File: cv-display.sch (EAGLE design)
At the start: 21 parts, among them IC1 TL072JD, IC2 TL072JD

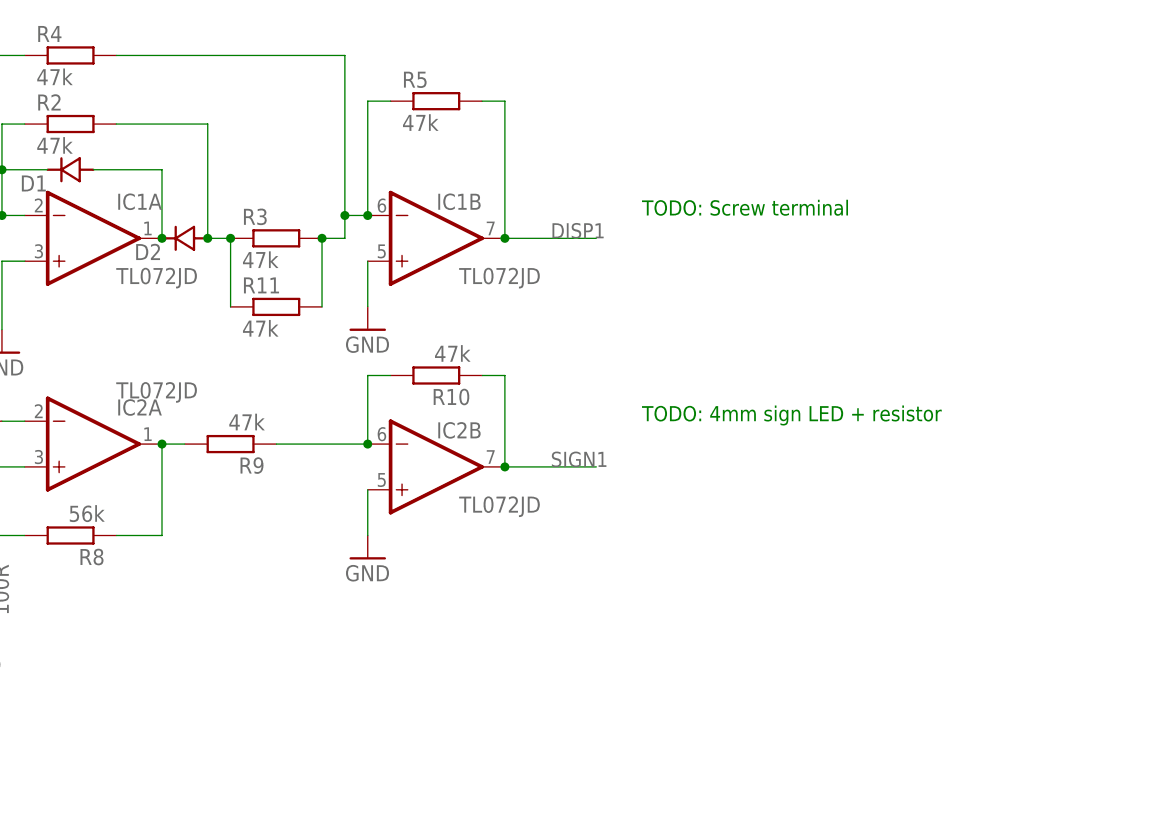
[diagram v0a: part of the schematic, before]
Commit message: Tested circuit, only missing screw terminals
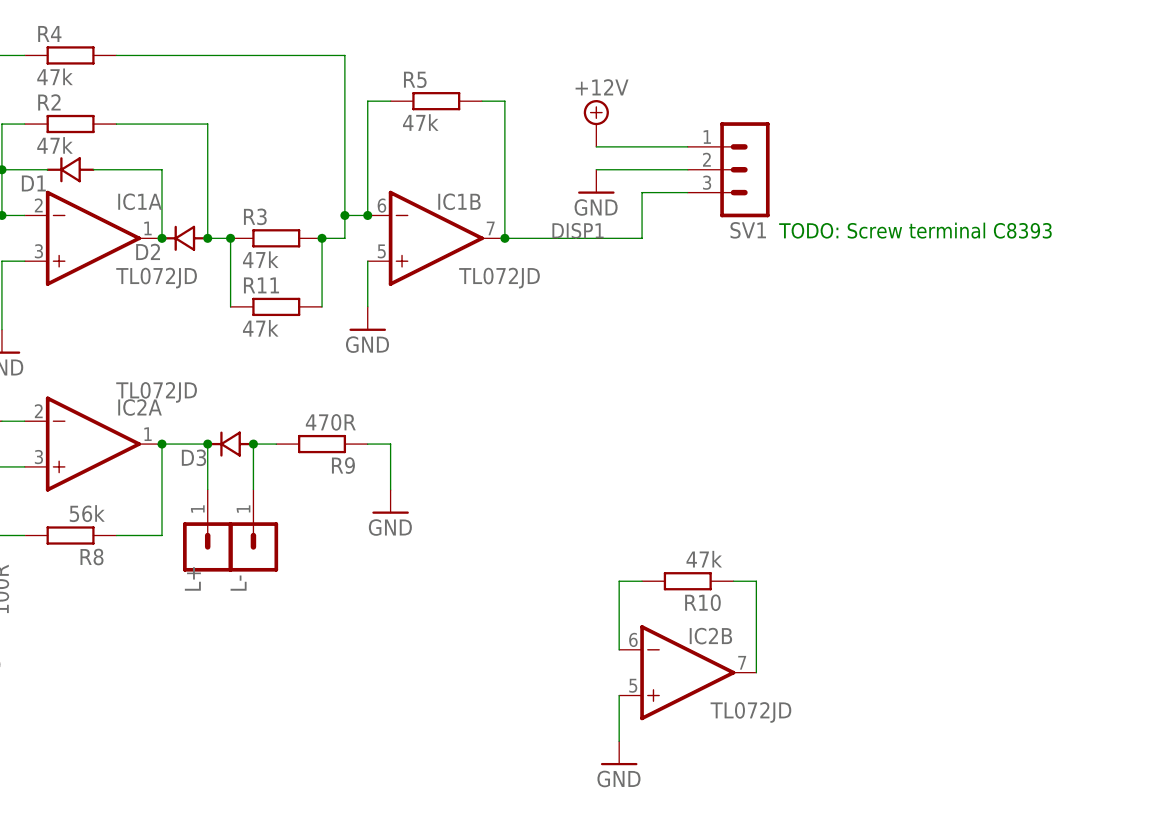
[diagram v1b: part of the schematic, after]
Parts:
- added D3: 1N4148SOD323, joakim:1N4148SOD323
- added L+, L-: (no value), joakim:MA01-1JN
- added SV1: (no value), joakim:MA03-1JC
- R9: value 47k -> 470R
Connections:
- net SIGN1 renamed N$11
- new net N$12: D3.A, L-.1, R9.2
- net +12V: now also SV1.1
- net DISP1: now also SV1.3
- net GND: now also R9.1, SV1.2
- net N$10: no longer R9.1
- net N$6: now also D3.C, L+.1; no longer R9.2
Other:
- note added: "TODO: Screw terminal C8393"
- note removed: "TODO: 4mm sign LED + resistor"
- note removed: "TODO: Screw terminal"
- moved on the sheet: IC2B, R10, R9

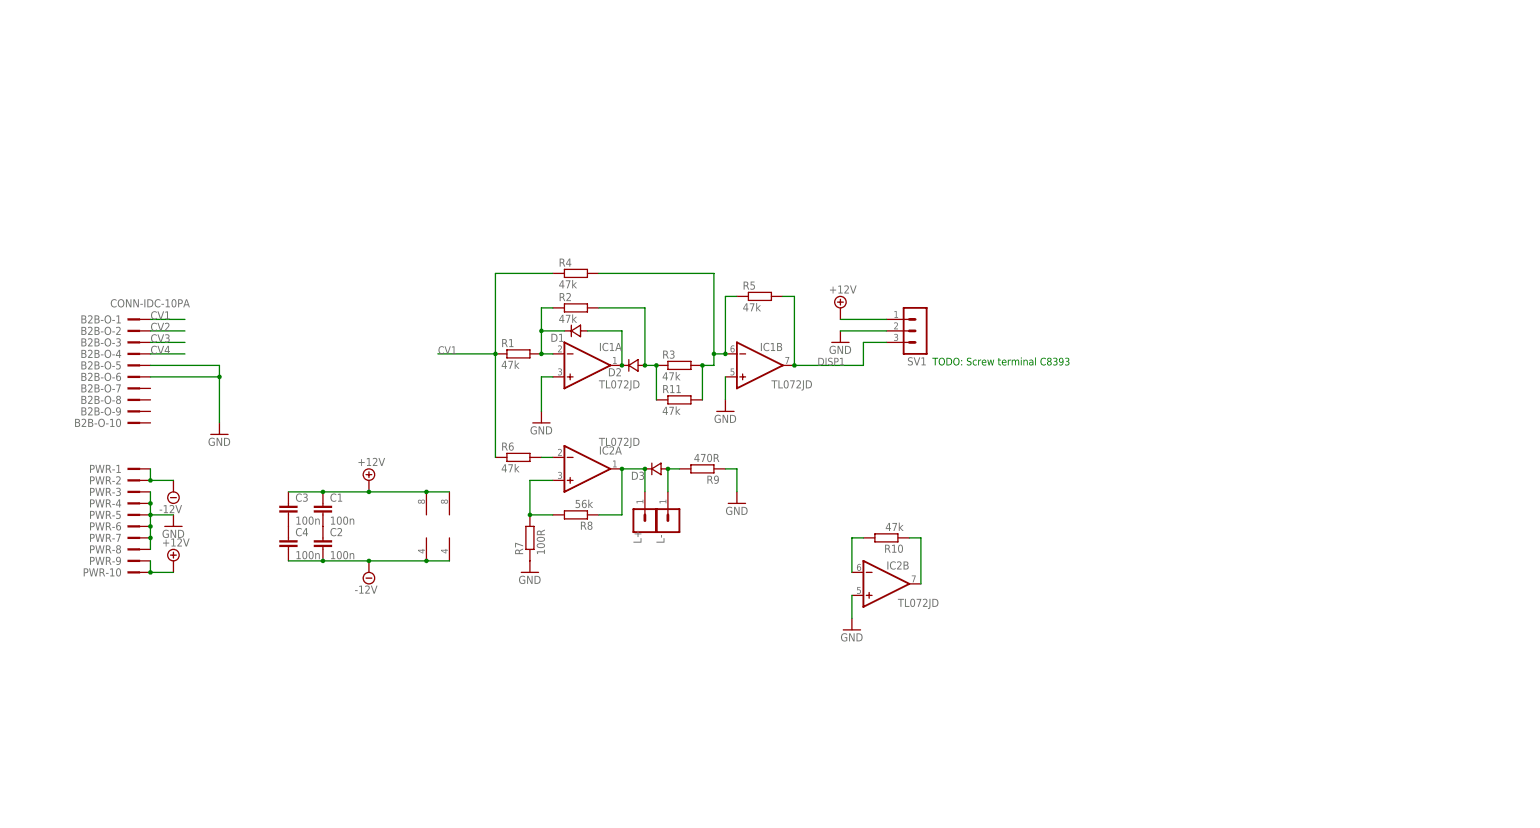
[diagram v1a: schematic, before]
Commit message: Traced almost everything
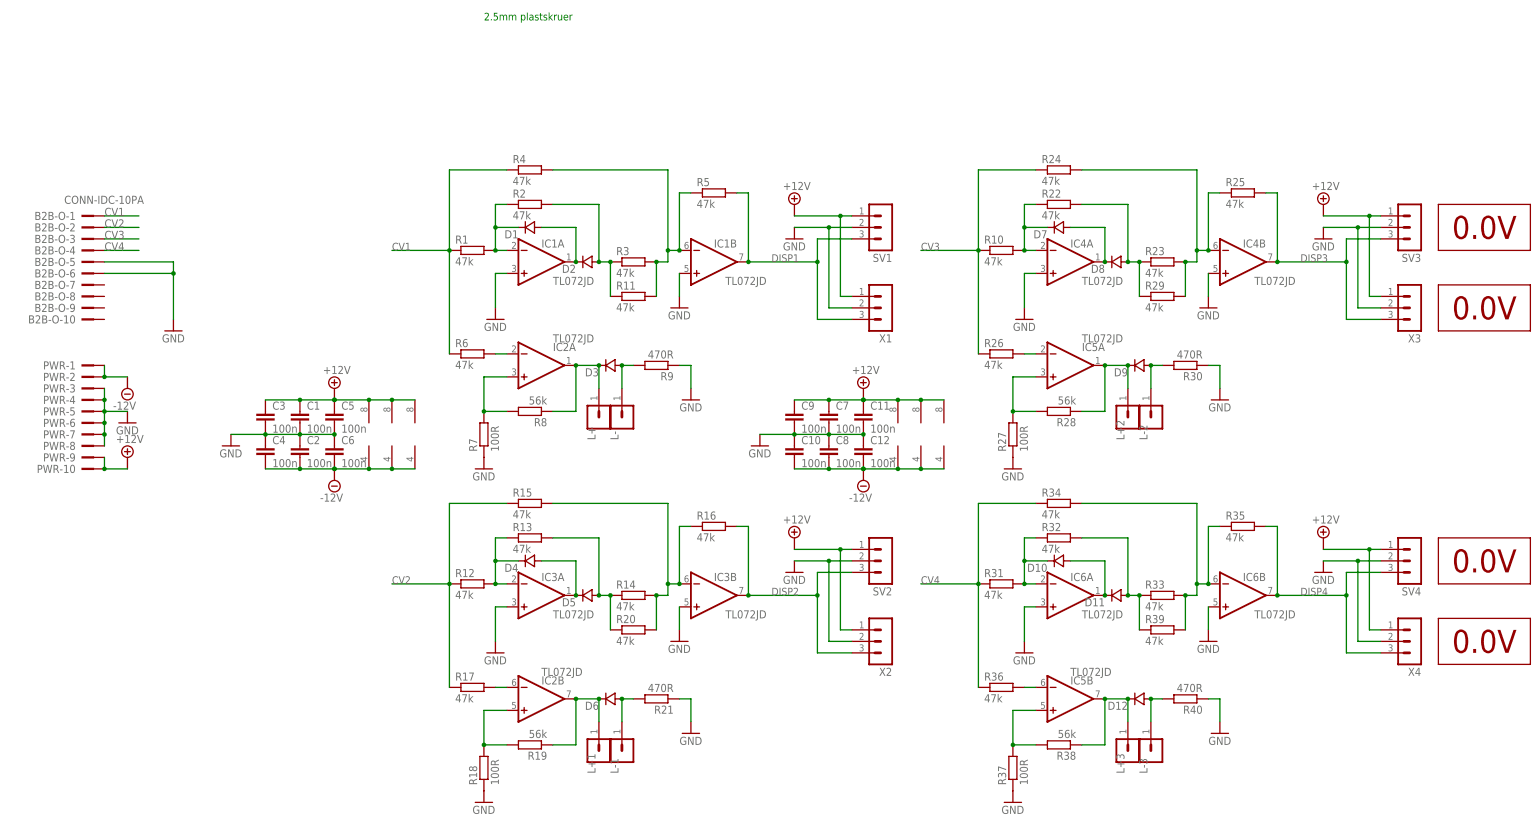
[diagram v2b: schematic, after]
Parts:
- added C10, C11, C12, C5, C6, C7, C8, C9: 100n, rcl:C-EUC0603
- added D10, D11, D12, D4, D5, D6, D7, D8, D9: 1N4148SOD323, joakim:1N4148SOD323
- added IC10, IC7, IC8, IC9: VOLTMETER, joakim:VOLTMETER
- added IC3, IC4, IC5, IC6: TL072JD, joakim:TL072JD
- added L+1, L+2, L+3, L-1, L-2, L-3: (no value), joakim:MA01-1JN
- added R12, R13, R14, R15, R16, R17, R20, R22, R23, R24, R25, R26, R29, R31, R32, R33, R34, R35, R36, R39: 47k, rcl:R-EU_R0603
- added R18, R27, R37: 100R, rcl:R-EU_R0603
- added R19, R28, R38: 56k, rcl:R-EU_R0603
- added R21, R30, R40: 470R, rcl:R-EU_R0603
- added SV2, SV3, SV4: (no value), joakim:MA03-1JC
- added X1, X2, X3, X4: WJ300V-5.0-3P, joakim:WJ300V-5.0-3P
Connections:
- new net DISP2: IC3B.OUT, R16.2, SV2.3, X2.3
- new net DISP3: IC4B.OUT, R25.2, SV3.3, X3.3
- new net DISP4: IC6B.OUT, R35.2, SV4.3, X4.3
- new net N$13: D4.C, IC3A.-IN, R12.2, R13.1
- new net N$14: D4.A, D5.C, IC3A.OUT
- new net N$15: D5.A, R13.2, R14.1, R20.1
- new net N$16: IC3B.-IN, R14.2, R15.2, R16.1, R20.2
- new net N$17: IC2B.-IN, R17.2
- new net N$18: IC2B.+IN, R18.2, R19.2
- new net N$19: D6.C, IC2B.OUT, L+1.1, R19.1
- new net N$20: D6.A, L-1.1, R21.2
- new net N$21: IC5A.-IN, R26.2
- new net N$22: IC5A.+IN, R27.2, R28.2
- new net N$23: D9.C, IC5A.OUT, L+2.1, R28.1
- new net N$24: D9.A, L-2.1, R30.2
- new net N$25: D10.C, IC6A.-IN, R31.2, R32.1
- new net N$26: D10.A, D11.C, IC6A.OUT
- new net N$27: D11.A, R32.2, R33.1, R39.1
- new net N$28: IC6B.-IN, R33.2, R34.2, R35.1, R39.2
- new net N$29: IC5B.-IN, R36.2
- new net N$30: IC5B.+IN, R37.2, R38.2
- new net N$31: D12.C, IC5B.OUT, L+3.1, R38.1
- new net N$32: D12.A, L-3.1, R40.2
- net +12V: now also C11.1, C5.1, C7.1, C9.1, IC3P.V+, IC4P.V+, IC5P.V+, IC6P.V+, SV2.1, SV3.1, SV4.1, X1.1, X2.1, X3.1, X4.1
- net -12V: now also C10.2, C12.2, C6.2, C8.2, IC3P.V-, IC4P.V-, IC5P.V-, IC6P.V-
- net CV2: now also R12.1, R15.1, R17.1
- net CV3: now also R10.1, R24.1, R26.1
- net CV4: now also R31.1, R34.1, R36.1
- net DISP1: now also X1.3
- net GND: now also C1.2, C10.1, C11.2, C12.1, C2.1, C3.2, C4.1, C5.2, C6.1, C7.2, C8.1, C9.2, IC3A.+IN, IC3B.+IN, IC4A.+IN, IC4B.+IN, IC6A.+IN, IC6B.+IN, R18.1, R21.1, R27.1, R30.1, R37.1, R40.1, SV2.2, SV3.2, SV4.2, X1.2, X2.2, X3.2, X4.2; no longer IC2B.+IN
- net N$10: now also D8.A, R22.2, R23.1, R29.1; no longer IC2B.-IN, R10.2
- net N$11: now also IC4B.-IN, R23.2, R24.2, R25.1, R29.2; no longer IC2B.OUT, R10.1
- net N$5: now also D7.C, IC4A.-IN, R10.2, R22.1; no longer C1.2, C2.1
- net N$7: now also D7.A, D8.C, IC4A.OUT; no longer C3.2, C4.1
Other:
- note added: "2.5mm plastskruer"
- note removed: "TODO: Screw terminal C8393"
- moved on the sheet: B2B-O-1, B2B-O-10, B2B-O-2, B2B-O-3, B2B-O-4, B2B-O-5, B2B-O-6, B2B-O-7, B2B-O-8, B2B-O-9, C1, C2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

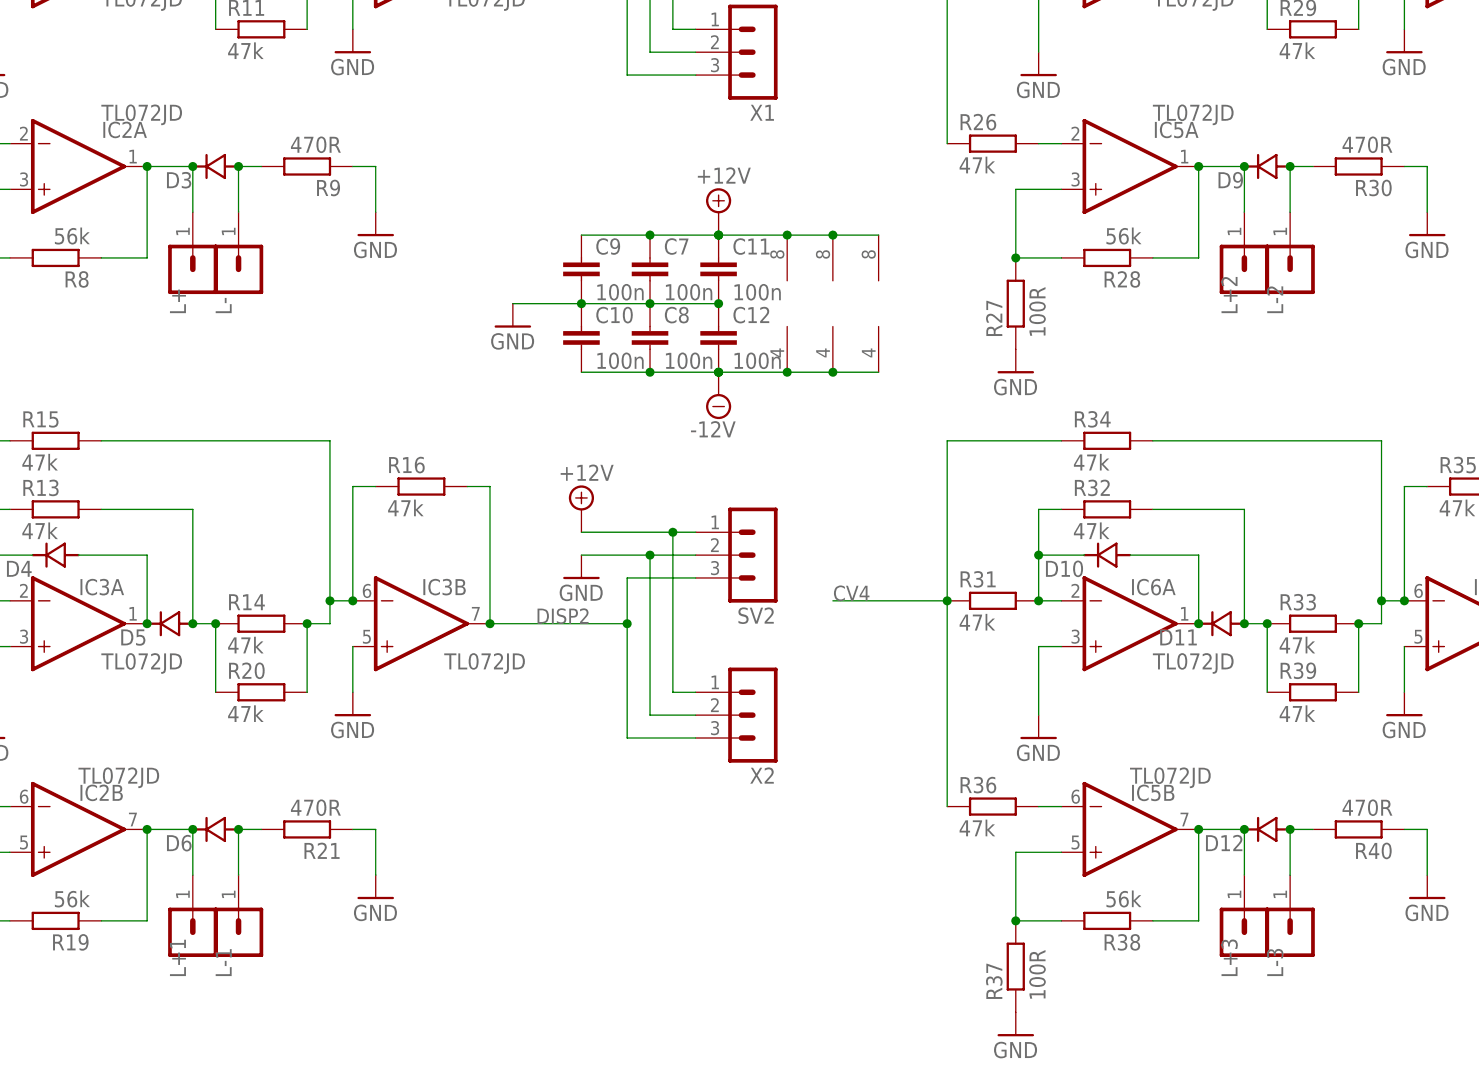
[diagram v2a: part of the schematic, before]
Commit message: Fixed leds and display sizes
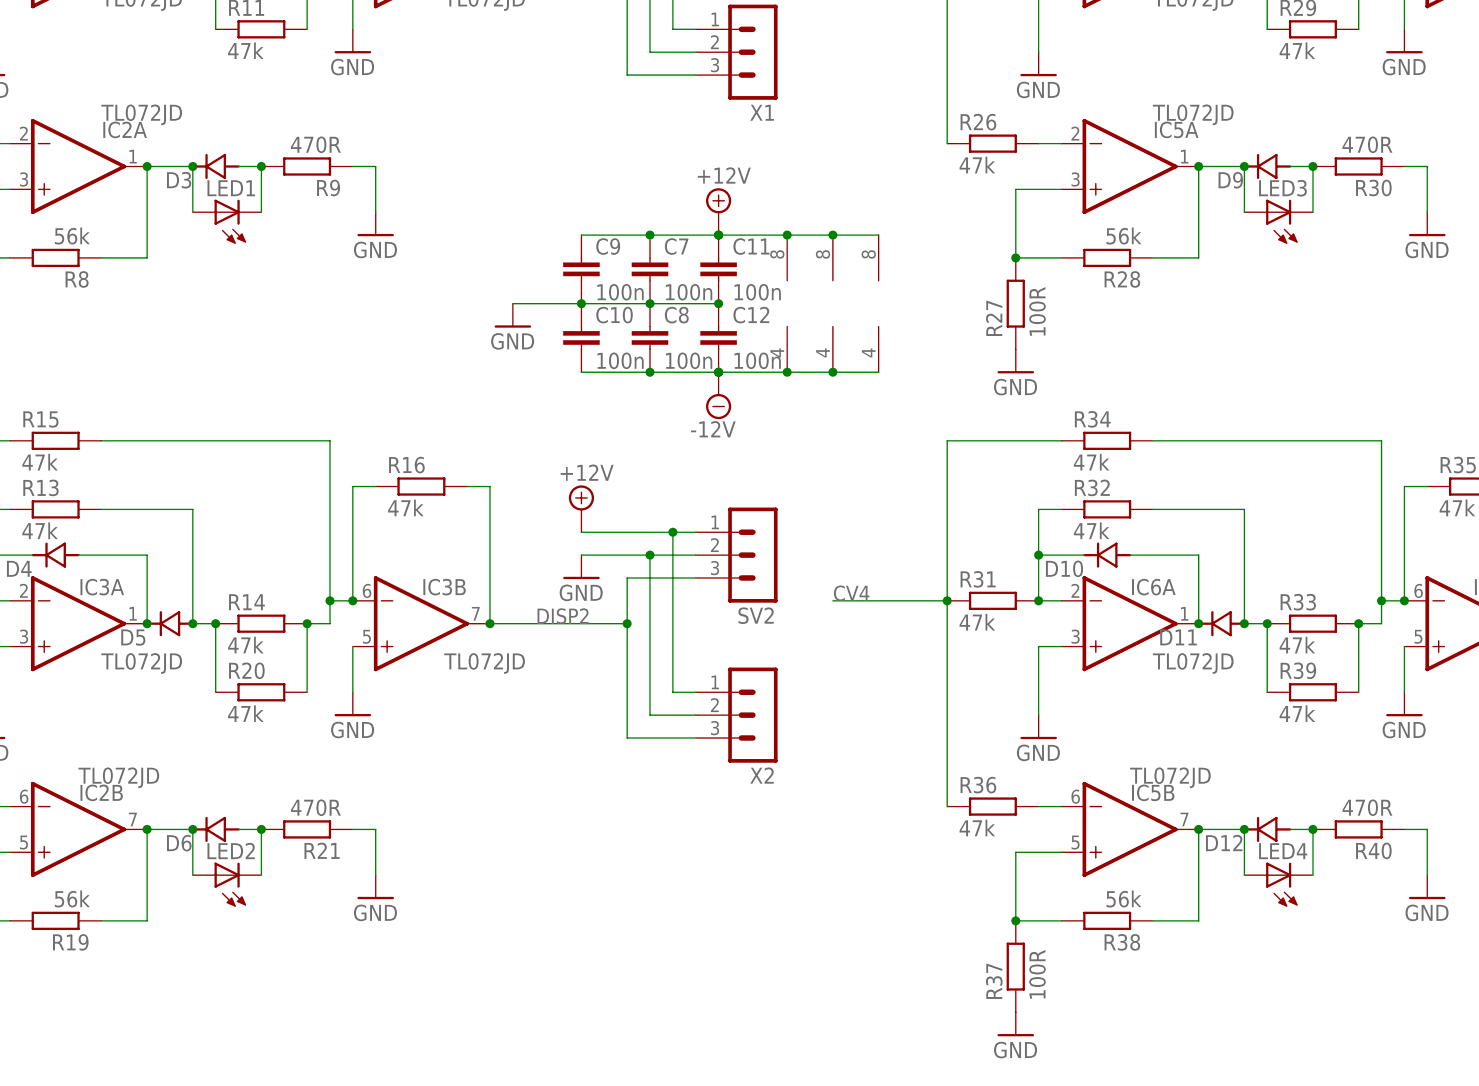
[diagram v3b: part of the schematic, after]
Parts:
- removed L+, L+1, L+2, L+3, L-, L-1, L-2, L-3: (no value), joakim:MA01-1JN
- added LED1, LED2, LED3, LED4: (no value), joakim-old:LED_J2X4
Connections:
- net N$12: now also LED1.C; no longer L-.1
- net N$19: now also LED2.A; no longer L+1.1
- net N$20: now also LED2.C; no longer L-1.1
- net N$23: now also LED3.A; no longer L+2.1
- net N$24: now also LED3.C; no longer L-2.1
- net N$31: now also LED4.A; no longer L+3.1
- net N$32: now also LED4.C; no longer L-3.1
- net N$6: now also LED1.A; no longer L+.1
